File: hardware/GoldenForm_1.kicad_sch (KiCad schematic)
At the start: 28 parts, among them IC1 UVLO, J1 SD_Socket, J2 USB_C_Receptacle_USB2.0_14P, J3 Conn_01x04_Pin, SW1 BOOT, SW2 RESET, U1 Buck_Boost, U2 BNO055, U4 ESP32-S3-WROOM-1

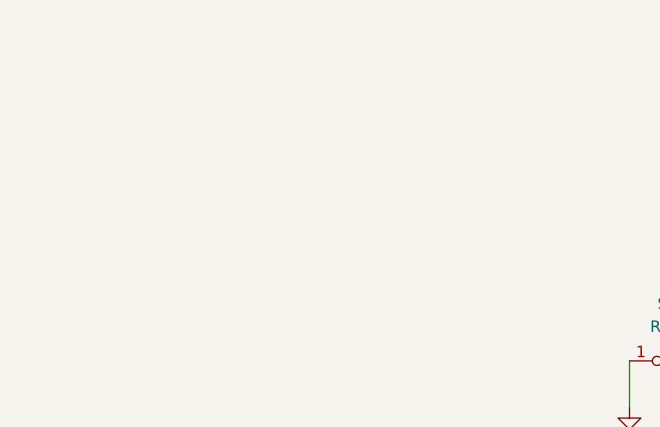
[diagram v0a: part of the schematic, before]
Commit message: added mounting holes to sch
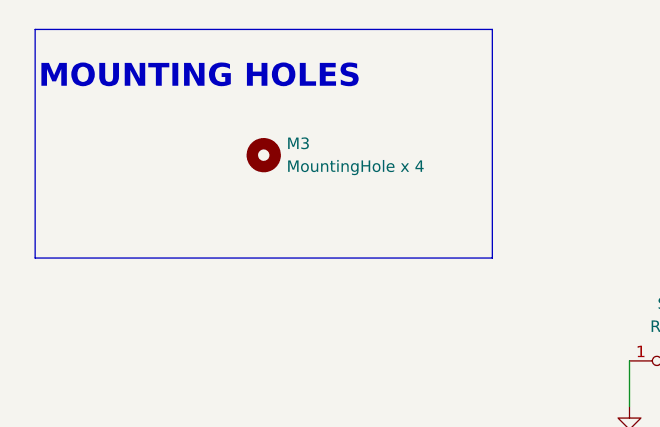
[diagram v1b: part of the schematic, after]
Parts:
- added M3: MountingHole x 4, MountingHole:MountingHole_3.2mm_M3, symbol Mechanical:MountingHole
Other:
- note added: "MOUNTING HOLES"
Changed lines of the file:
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@@
 	)
 	(rectangle
+		(start 12.7 12.7)
+		(end 63.5 38.1)
+		(stroke
+			(width 0)
+			(type default)
+		)
+		(fill
+			(type none)
+		)
+	)
+	(rectangle
 		(start 200.66 81.28)
 		(end 284.48 165.1)
@@
 		)
 	)
+	(text "MOUNTING HOLES"
+		(exclude_from_sim no)
+		(at 30.988 18.034 0)
+		(effects
+			(font
+				(size 2.54 2.54)
+				(thickness 0.254)
+				(bold yes)
+			)
+		)
+	)
 	(junction
 		(at 214.63 138.43)
@@
 					(unit 1)
 				)
+			)
+		)
+	)
+	(symbol
+		(lib_id "Mechanical:MountingHole")
+		(at 38.1 26.67 0)
+		(unit 1)
+		(exclude_from_sim no)
+		(in_bom no)
+		(on_board yes)
+		(dnp no)
+		(fields_autoplaced yes)
+		(property "Reference" "M3"
+			(at 40.64 25.3999 0)
+			(effects
+				(font
+					(size 1.27 1.27)
+				)
+				(justify left)
+			)
+		)
+		(property "Value" "MountingHole x 4"
+			(at 40.64 27.9399 0)
+			(effects
+				(font
+					(size 1.27 1.27)
+				)
+				(justify left)
+			)
+		)
+		(property "Footprint" "MountingHole:MountingHole_3.2mm_M3"
+			(at 38.1 26.67 0)
+			(effects
+				(font
+					(size 1.27 1.27)
+				)
+				(hide yes)
+			)
+		)
+		(property "Datasheet" "~"
+			(at 38.1 26.67 0)
+			(effects
+				(font
+					(size 1.27 1.27)
+				)
+				(hide yes)
+			)
+		)
+		(property "Description" "Mounting Hole without connection"
+			(at 38.1 26.67 0)
+			(effects
+				(font
+					(size 1.27 1.27)
+				)
+				(hide yes)
+			)
+		)
+		(instances
+			(project ""
+				(path "/64cfd788-f968-4e49-826d-6322743ab44f"
+					(reference "M3")
+					(unit 1)
+				)

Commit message: some new changes
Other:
- moved on the sheet: C1

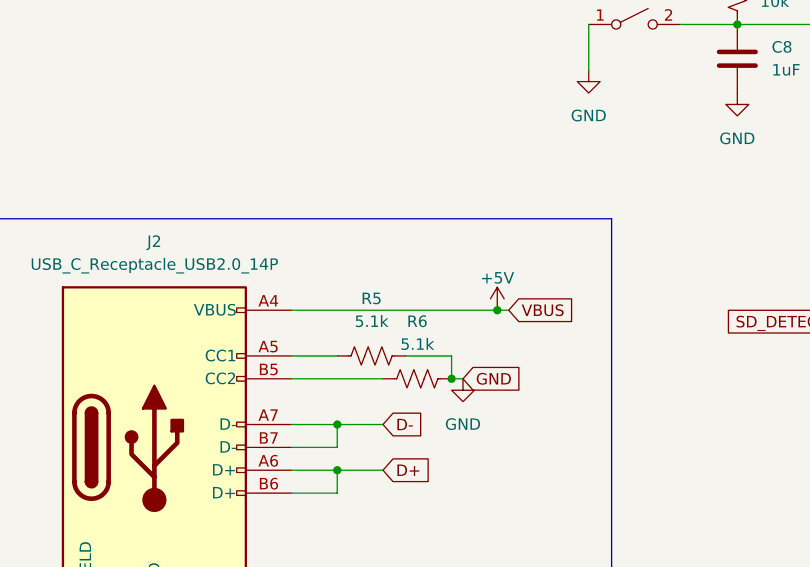
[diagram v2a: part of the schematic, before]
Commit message: more changes for ERC cleanup
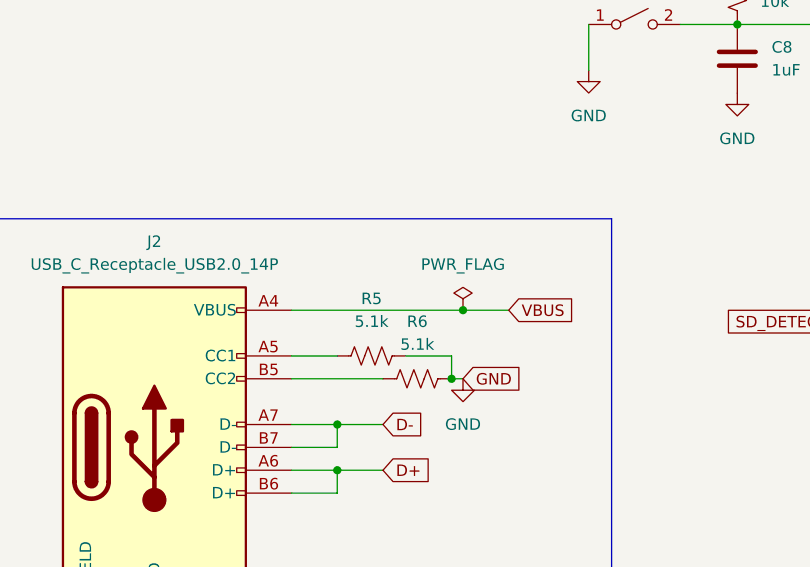
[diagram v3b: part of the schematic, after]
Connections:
- net +5V renamed VBUS
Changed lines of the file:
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@@
 	)
 	(junction
-		(at 68.58 81.28)
-		(diameter 0)
-		(color 0 0 0 0)
-	)
-	(junction
 		(at 143.51 100.33)
 		(diameter 0)
@@
 	)
 	(junction
+		(at 64.77 81.28)
+		(diameter 0)
+		(color 0 0 0 0)
+	)
+	(junction
 		(at 50.8 99.06)
 		(diameter 0)
@@
 	(wire
 		(pts
-			(xy 68.58 81.28) (xy 69.85 81.28)
-		)
-		(stroke
-			(width 0)
-			(type default)
-		)
-	)
-	(wire
-		(pts
 			(xy 64.77 88.9) (xy 63.5 88.9)
 		)
@@
 	(wire
 		(pts
+			(xy 64.77 81.28) (xy 69.85 81.28)
+		)
+		(stroke
+			(width 0)
+			(type default)
+		)
+	)
+	(wire
+		(pts
 			(xy 214.63 128.27) (xy 224.79 128.27)
 		)
@@
 	(wire
 		(pts
-			(xy 45.72 81.28) (xy 68.58 81.28)
+			(xy 45.72 81.28) (xy 64.77 81.28)
 		)
 		(stroke
@@
 	)
 	(symbol
-		(lib_id "power:+5V")
-		(at 68.58 81.28 0)
-		(unit 1)
-		(exclude_from_sim no)
-		(in_bom yes)
-		(on_board yes)
-		(dnp no)
-		(property "Reference" "#PWR013"
-			(at 68.58 85.09 0)
-			(effects
-				(font
-					(size 1.27 1.27)
-				)
-				(hide yes)
-			)
-		)
-		(property "Value" "+5V"
-			(at 68.58 77.724 0)
-			(effects
-				(font
-					(size 1.27 1.27)
-				)
-			)
-		)
-		(property "Footprint" ""
-			(at 68.58 81.28 0)
-			(effects
-				(font
-					(size 1.27 1.27)
-				)
-				(hide yes)
-			)
-		)
-		(property "Datasheet" ""
-			(at 68.58 81.28 0)
-			(effects
-				(font
-					(size 1.27 1.27)
-				)
-				(hide yes)
-			)
-		)
-		(property "Description" "Power symbol creates a global label with name \"+5V\""
-			(at 68.58 81.28 0)
-			(effects
-				(font
-					(size 1.27 1.27)
-				)
-				(hide yes)
-			)
-		)
-		(pin "1"
-		)
-		(instances
-			(project ""
-				(path "/64cfd788-f968-4e49-826d-6322743ab44f"
-					(reference "#PWR013")
-					(unit 1)
-				)
-			)
-		)
-	)
-	(symbol
 		(lib_id "Switch:SW_SPST")
 		(at 123.19 54.61 0)
@@
 					(unit 1)
 				)
+			)
+		)
+	)
+	(symbol
+		(lib_id "power:PWR_FLAG")
+		(at 64.77 81.28 0)
+		(unit 1)
+		(exclude_from_sim no)
+		(in_bom yes)
+		(on_board yes)
+		(dnp no)
+		(fields_autoplaced yes)
+		(property "Reference" "#FLG02"
+			(at 64.77 79.375 0)
+			(effects
+				(font
+					(size 1.27 1.27)
+				)
+				(hide yes)
+			)
+		)
+		(property "Value" "PWR_FLAG"
+			(at 64.77 76.2 0)
+			(effects
+				(font
+					(size 1.27 1.27)
+				)
+			)
+		)
+		(property "Footprint" ""
+			(at 64.77 81.28 0)
+			(effects
+				(font
+					(size 1.27 1.27)
+				)
+				(hide yes)
+			)
+		)
+		(property "Datasheet" "~"
+			(at 64.77 81.28 0)
+			(effects
+				(font
+					(size 1.27 1.27)
+				)
+				(hide yes)
+			)
+		)
+		(property "Description" "Special symbol for telling ERC where power comes from"
+			(at 64.77 81.28 0)
+			(effects
+				(font
+					(size 1.27 1.27)
+				)
+				(hide yes)
+			)
+		)
+		(pin "1"
+		)
+		(instances
+			(project ""
+				(path "/64cfd788-f968-4e49-826d-6322743ab44f"
+					(reference "#FLG02")
+					(unit 1)
+				)

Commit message: wip
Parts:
- added D2: LED, symbol Device:LED
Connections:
- net LED_4: now reaches U4.17 (IO9)
- net LED_1: no longer names the net of U4.39 (IO1)
- net LED_1: now also D2.2 (A)
- no-connect marks 15 -> 14
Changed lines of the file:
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@@
 	)
 	(no_connect
-		(at 128.27 77.47)
-	)
-	(no_connect
 		(at 128.27 87.63)
 	)
@@
 	(wire
 		(pts
+			(xy 123.19 44.45) (xy 127 44.45)
+		)
+		(stroke
+			(width 0)
+			(type default)
+		)
+	)
+	(wire
+		(pts
 			(xy 45.72 99.06) (xy 50.8 99.06)
 		)
@@
 	(wire
 		(pts
+			(xy 127 44.45) (xy 127 57.15)
+		)
+		(stroke
+			(width 0)
+			(type default)
+		)
+	)
+	(wire
+		(pts
 			(xy 139.7 100.33) (xy 143.51 100.33)
 		)
@@
 	(wire
 		(pts
+			(xy 127 57.15) (xy 128.27 57.15)
+		)
+		(stroke
+			(width 0)
+			(type default)
+		)
+	)
+	(wire
+		(pts
 			(xy 105.41 49.53) (xy 128.27 49.53)
 		)
@@
 	(wire
 		(pts
+			(xy 121.92 77.47) (xy 128.27 77.47)
+		)
+		(stroke
+			(width 0)
+			(type default)
+		)
+	)
+	(wire
+		(pts
 			(xy 101.6 151.13) (xy 100.33 151.13)
 		)
@@
 		)
 	)
+	(global_label "LED_4"
+		(shape input)
+		(at 121.92 77.47 180)
+		(fields_autoplaced yes)
+		(effects
+			(font
+				(size 1.27 1.27)
+			)
+			(justify right)
+		)
+		(property "Intersheetrefs" "${INTERSHEET_REFS}"
+			(at 113.3106 77.47 0)
+			(effects
+				(font
+					(size 1.27 1.27)
+				)
+				(justify right)
+				(hide yes)
+			)
+		)
+	)
 	(global_label "UART_RX"
 		(shape input)
@@
 		)
 	)
-	(global_label "LED_1"
-		(shape input)
-		(at 128.27 57.15 180)
-		(fields_autoplaced yes)
-		(effects
-			(font
-				(size 1.27 1.27)
-			)
-			(justify right)
-		)
-		(property "Intersheetrefs" "${INTERSHEET_REFS}"
-			(at 119.6606 57.15 0)
-			(effects
-				(font
-					(size 1.27 1.27)
-				)
-				(justify right)
-				(hide yes)
-			)
-		)
-	)
 	(global_label "GND"
 		(shape input)
@@
 					(unit 1)
 				)
+			)
+		)
+	)
+	(symbol
+		(lib_id "Device:LED")
+		(at 119.38 44.45 0)
+		(unit 1)
+		(exclude_from_sim no)
+		(in_bom yes)
+		(on_board yes)
+		(dnp no)
+		(fields_autoplaced yes)
+		(property "Reference" "D2"
+			(at 117.7925 38.1 0)
+			(effects
+				(font
+					(size 1.27 1.27)
+				)
+			)
+		)
+		(property "Value" "LED"
+			(at 117.7925 40.64 0)
+			(effects
+				(font
+					(size 1.27 1.27)
+				)
+			)
+		)
+		(property "Footprint" ""
+			(at 119.38 44.45 0)
+			(effects
+				(font
+					(size 1.27 1.27)
+				)
+				(hide yes)
+			)
+		)
+		(property "Datasheet" "~"
+			(at 119.38 44.45 0)
+			(effects
+				(font
+					(size 1.27 1.27)
+				)
+				(hide yes)
+			)
+		)
+		(property "Description" "Light emitting diode"
+			(at 119.38 44.45 0)
+			(effects
+				(font
+					(size 1.27 1.27)
+				)
+				(hide yes)
+			)
+		)
+		(property "Sim.Pins" "1=K 2=A"
+			(at 119.38 44.45 0)
+			(effects
+				(font
+					(size 1.27 1.27)
+				)
+				(hide yes)
+			)
+		)
+		(pin "1"
+		)
+		(pin "2"
+		)
+		(instances
+			(project "GoldenForm_1"
+				(path "/64cfd788-f968-4e49-826d-6322743ab44f"
+					(reference "D2")
+					(unit 1)
+				)
